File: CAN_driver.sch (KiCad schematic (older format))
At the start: 28 parts, among them J3 DB9_Male, J4 DB9_Male, J5 DB9_Male, J6 DB9_Male, U3 TCAN1042HVD, U5 TCAN1042HVD

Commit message: forgot to save schematic
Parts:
- J3, J4, J5, J6: footprint Connector_Dsub:DSUB-9_Male_Horizontal_P2.77x2.84mm_EdgePinOffset7.70mm_Housed_MountingHolesOffset9.12mm -> Connector_Dsub:DSUB-9_Male_Vertical_P2.77x2.84mm_MountingHoles
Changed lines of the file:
@@
 F 0 "J5" H 8130 4346 50  0000 L CNN
 F 1 "DB9_Male" H 8130 4255 50  0000 L CNN
-F 2 "Connector_Dsub:DSUB-9_Male_Horizontal_P2.77x2.84mm_EdgePinOffset7.70mm_Housed_MountingHolesOffset9.12mm" H 7950 4300 50  0001 C CNN
+F 2 "Connector_Dsub:DSUB-9_Male_Vertical_P2.77x2.84mm_MountingHoles" H 7950 4300 50  0001 C CNN
 F 3 " ~" H 7950 4300 50  0001 C CNN
 F 4 "5747840-3" H 7950 4300 50  0001 C CNN "Part"
@@
 F 0 "J6" H 8130 5496 50  0000 L CNN
 F 1 "DB9_Male" H 8130 5405 50  0000 L CNN
-F 2 "Connector_Dsub:DSUB-9_Male_Horizontal_P2.77x2.84mm_EdgePinOffset7.70mm_Housed_MountingHolesOffset9.12mm" H 7950 5450 50  0001 C CNN
+F 2 "Connector_Dsub:DSUB-9_Male_Vertical_P2.77x2.84mm_MountingHoles" H 7950 5450 50  0001 C CNN
 F 3 " ~" H 7950 5450 50  0001 C CNN
 F 4 "5747840-3" H 7950 5450 50  0001 C CNN "Part"
@@
 F 0 "J4" H 8130 2496 50  0000 L CNN
 F 1 "DB9_Male" H 8130 2405 50  0000 L CNN
-F 2 "Connector_Dsub:DSUB-9_Male_Horizontal_P2.77x2.84mm_EdgePinOffset7.70mm_Housed_MountingHolesOffset9.12mm" H 7950 2450 50  0001 C CNN
+F 2 "Connector_Dsub:DSUB-9_Male_Vertical_P2.77x2.84mm_MountingHoles" H 7950 2450 50  0001 C CNN
 F 3 " ~" H 7950 2450 50  0001 C CNN
 F 4 "5747840-3" H 7950 2450 50  0001 C CNN "Part"
@@
 F 0 "J3" H 8130 1346 50  0000 L CNN
 F 1 "DB9_Male" H 8130 1255 50  0000 L CNN
-F 2 "Connector_Dsub:DSUB-9_Male_Horizontal_P2.77x2.84mm_EdgePinOffset7.70mm_Housed_MountingHolesOffset9.12mm" H 7950 1300 50  0001 C CNN
+F 2 "Connector_Dsub:DSUB-9_Male_Vertical_P2.77x2.84mm_MountingHoles" H 7950 1300 50  0001 C CNN
 F 3 " ~" H 7950 1300 50  0001 C CNN
 F 4 "5747840-3" H 7950 1300 50  0001 C CNN "Part"

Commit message: decouple caps, moved testpoint for usb access, tcan footprints
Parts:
- U3, U5: footprint Package_SO:SOIC-8-1EP_3.9x4.9mm_P1.27mm_EP2.41x3.81mm -> Package_SO:SO-8_3.9x4.9mm_P1.27mm
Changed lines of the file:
@@
 BBCAN+
-$Comp
-L TCAN:TCAN1042HVD U3
-U 1 1 5E4AADCC
-P 3650 1300
-F 0 "U3" H 4450 1687 60  0000 C CNN
-F 1 "TCAN1042HVD" H 4450 1581 60  0000 C CNN
-F 2 "Package_SO:SOIC-8-1EP_3.9x4.9mm_P1.27mm_EP2.41x3.81mm" H 4450 1540 60  0001 C CNN
-F 3 "" H 3650 1300 60  0000 C CNN
-F 4 "296-48672-1-ND" H 3650 1300 50  0001 C CNN "Part"
-	1    3650 1300
-	1    0    0    -1
-$EndComp
 $Comp
 L power:GNDD #PWR?
@@
 F 0 "U5" H 4450 4587 60  0000 C CNN
 F 1 "TCAN1042HVD" H 4450 4481 60  0000 C CNN
-F 2 "Package_SO:SOIC-8-1EP_3.9x4.9mm_P1.27mm_EP2.41x3.81mm" H 4450 4440 60  0001 C CNN
+F 2 "Package_SO:SO-8_3.9x4.9mm_P1.27mm" H 4450 4440 60  0001 C CNN
 F 3 "" H 3650 4200 60  0000 C CNN
 F 4 "296-48672-1-ND" H 3650 4200 50  0001 C CNN "Part"
@@
 	1    0    0    -1
 $EndComp
+$Comp
+L TCAN:TCAN1042HVD U3
+U 1 1 5E4AADCC
+P 3650 1300
+F 0 "U3" H 4450 1687 60  0000 C CNN
+F 1 "TCAN1042HVD" H 4450 1581 60  0000 C CNN
+F 2 "Package_SO:SO-8_3.9x4.9mm_P1.27mm" H 4450 1540 60  0001 C CNN
+F 3 "" H 3650 1300 60  0000 C CNN
+F 4 "296-48672-1-ND" H 3650 1300 50  0001 C CNN "Part"
+	1    3650 1300
+	1    0    0    -1
+$EndComp

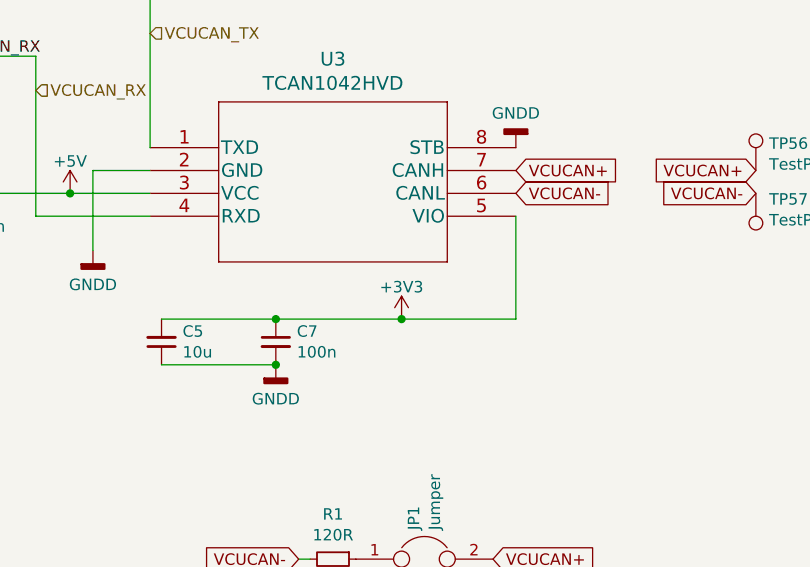
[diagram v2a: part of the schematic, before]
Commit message: better routing, tcan footprint, mount holes + silkscreen
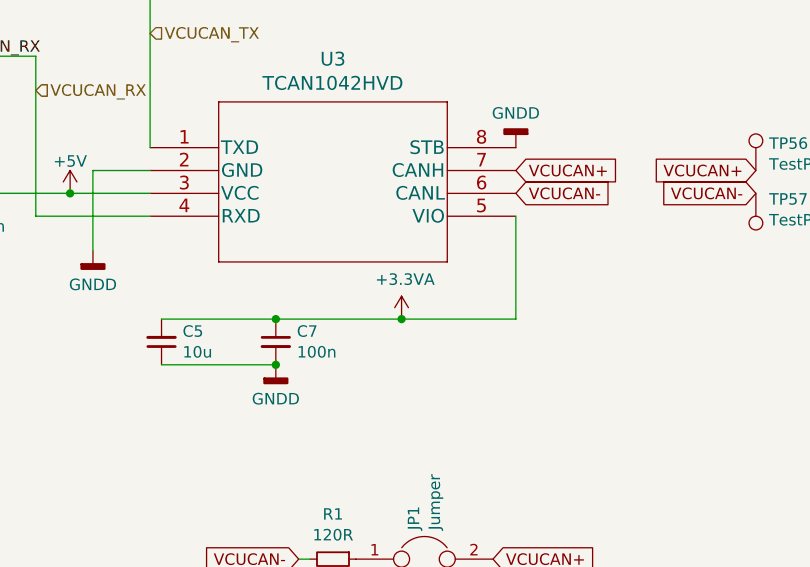
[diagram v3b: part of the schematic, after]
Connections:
- net +3V3: no longer C5.2, C7.1, U3.5 (VIO)
- new net +3.3VA: C5.2, C7.1, U3.5 (VIO)
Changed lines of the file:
@@
 $EndComp
 Connection ~ 4200 2050
-Connection ~ 4750 2050
 Wire Wire Line
 	2750 1500 3300 1500
@@
 Wire Wire Line
 	3650 1500 3300 1500
-$Comp
-L power:+3.3V #PWR?
-U 1 1 5E53D641
-P 4750 2050
-AR Path="/5E53D641" Ref="#PWR?"  Part="1"
-AR Path="/5ED986AC/5E53D641" Ref="#PWR0119"  Part="1"
-F 0 "#PWR0119" H 4750 1900 50  0001 C CNN
-F 1 "+3V3" H 4750 2190 50  0000 C CNN
-F 2 "" H 4750 2050 60  0000 C CNN
-F 3 "" H 4750 2050 60  0000 C CNN
-	1    4750 2050
-	1    0    0    -1
-$EndComp
 Text Label 2750 650  0    50   ~ 0
 VCUCAN_TX
@@
 VCUCAN_RX
 Wire Wire Line
-	4200 2050 4750 2050
-Wire Wire Line
 	5250 1600 5250 2050
-Wire Wire Line
-	4750 2050 5250 2050
 $Comp
 L power:GNDD #PWR?
@@
 $EndComp
 Connection ~ 4200 4950
-Connection ~ 4750 4950
 Wire Wire Line
 	2750 4400 3300 4400
@@
 Wire Wire Line
 	3650 4400 3300 4400
-$Comp
-L power:+3.3V #PWR?
-U 1 1 5E766408
-P 4750 4950
-AR Path="/5E766408" Ref="#PWR?"  Part="1"
-AR Path="/5ED986AC/5E766408" Ref="#PWR0131"  Part="1"
-F 0 "#PWR0131" H 4750 4800 50  0001 C CNN
-F 1 "+3V3" H 4750 5090 50  0000 C CNN
-F 2 "" H 4750 4950 60  0000 C CNN
-F 3 "" H 4750 4950 60  0000 C CNN
-	1    4750 4950
-	1    0    0    -1
-$EndComp
 Text Label 2750 3550 0    50   ~ 0
 BBCAN_TX
@@
 BBCAN_RX
 Wire Wire Line
-	4200 4950 4750 4950
-Wire Wire Line
 	5250 4500 5250 4950
-Wire Wire Line
-	4750 4950 5250 4950
 $Comp
 L power:GNDD #PWR?
@@
 	1    0    0    -1
 $EndComp
+Wire Wire Line
+	4750 4950 5250 4950
+Wire Wire Line
+	4200 4950 4750 4950
+Connection ~ 4750 4950
+$Comp
+L power:+3.3V #PWR?
+U 1 1 5E766408
+P 4750 4950
+AR Path="/5E766408" Ref="#PWR?"  Part="1"
+AR Path="/5ED986AC/5E766408" Ref="#PWR0131"  Part="1"
+F 0 "#PWR0131" H 4750 4800 50  0001 C CNN
+F 1 "+3V3" H 4750 5090 50  0000 C CNN
+F 2 "" H 4750 4950 60  0000 C CNN
+F 3 "" H 4750 4950 60  0000 C CNN
+	1    4750 4950
+	1    0    0    -1
+$EndComp
+Wire Wire Line
+	4200 2050 4750 2050
+$Comp
+L power:+3.3VA #PWR?
+U 1 1 5F34AABC
+P 4750 2050
+AR Path="/5F34AABC" Ref="#PWR?"  Part="1"
+AR Path="/5ED986AC/5F34AABC" Ref="#PWR0115"  Part="1"
+F 0 "#PWR0115" H 4750 1900 50  0001 C CNN
+F 1 "+3.3VA" H 4765 2223 50  0000 C CNN
+F 2 "" H 4750 2050 50  0001 C CNN
+F 3 "" H 4750 2050 50  0001 C CNN
+	1    4750 2050
+	1    0    0    -1
+$EndComp
+Connection ~ 4750 2050
+Wire Wire Line
+	4750 2050 5250 2050
 $EndSCHEMATC

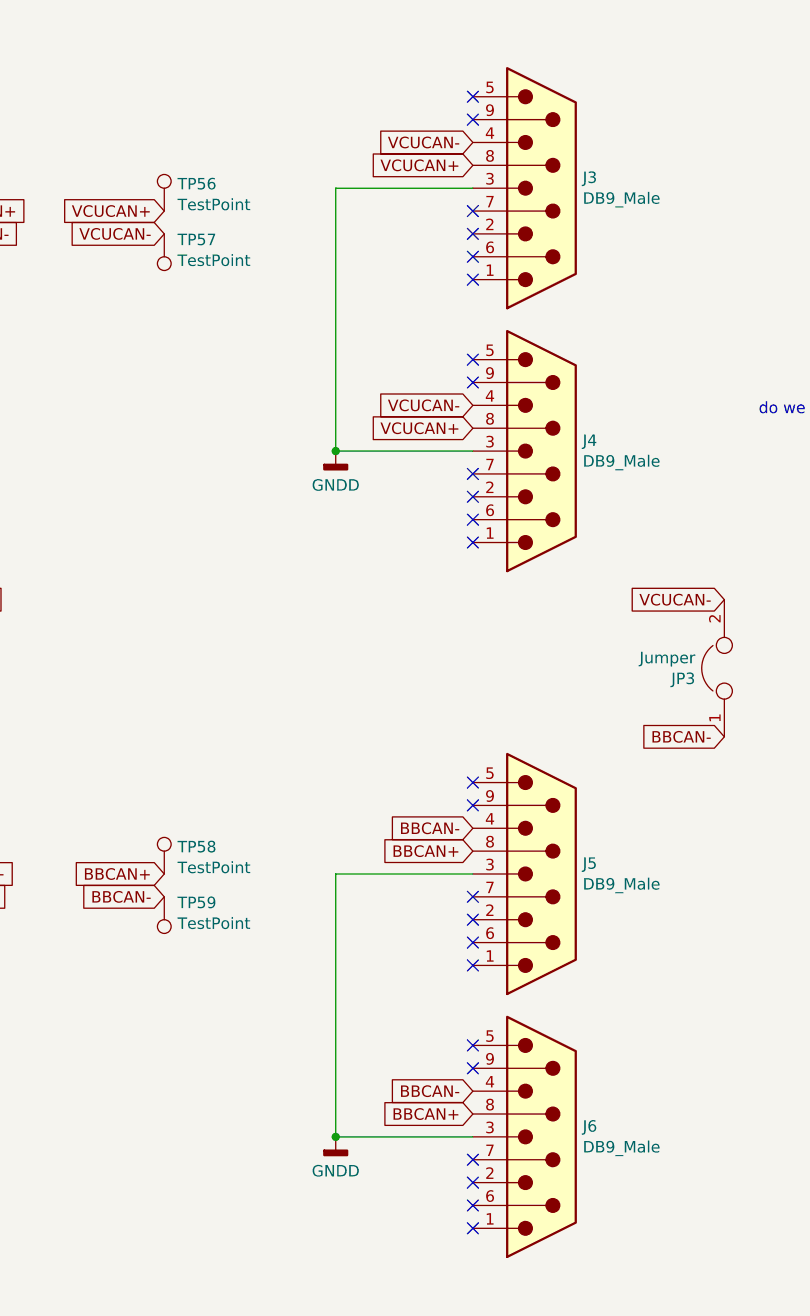
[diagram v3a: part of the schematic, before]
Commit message: rs232/can fix
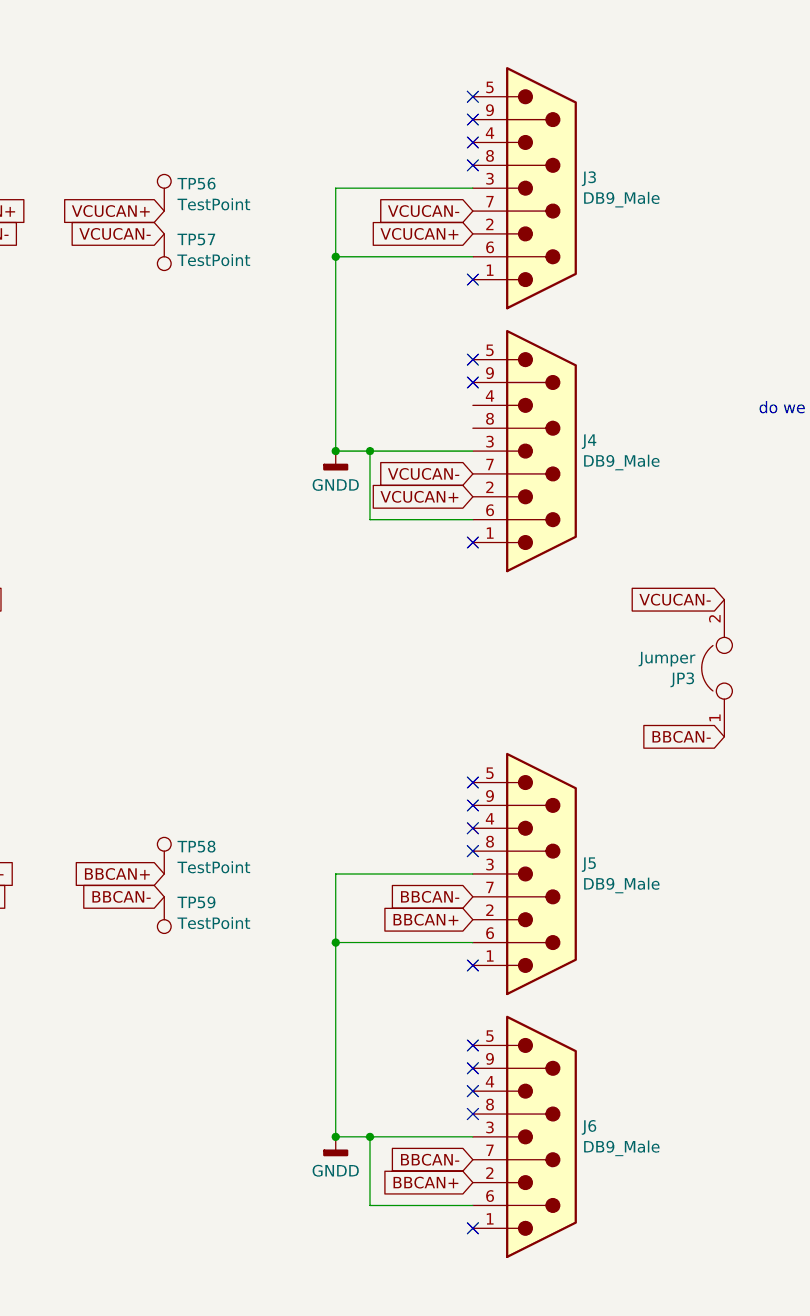
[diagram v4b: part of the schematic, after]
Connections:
- net BBCAN+: now also J5.2, J6.2; no longer J5.8, J6.8
- net BBCAN-: now also J5.7, J6.7; no longer J5.4, J6.4
- net GNDD: now also J3.6, J4.6, J5.6, J6.6
- net VCUCAN+: now also J3.2, J4.2; no longer J3.8, J4.8
- net VCUCAN-: now also J3.7, J4.7; no longer J3.4, J4.4
- no-connect marks 24 -> 18
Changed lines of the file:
@@
 VCUCAN+
 Wire Wire Line
-	7050 5450 7650 5450
+	7050 5450 7200 5450
 Wire Wire Line
 	7650 4300 7050 4300
-Text GLabel 7650 5350 0    50   Input ~ 0
+Text GLabel 7650 5650 0    50   Input ~ 0
 BBCAN+
-Text GLabel 7650 4200 0    50   Input ~ 0
+Text GLabel 7650 4500 0    50   Input ~ 0
 BBCAN+
-Text GLabel 7650 5250 0    50   Input ~ 0
+Text GLabel 7650 5550 0    50   Input ~ 0
 BBCAN-
-Text GLabel 7650 4100 0    50   Input ~ 0
+Text GLabel 7650 4400 0    50   Input ~ 0
 BBCAN-
 $Comp
@@
 	1    0    0    -1
 $EndComp
-Text GLabel 7650 1100 0    50   Input ~ 0
+Text GLabel 7650 1400 0    50   Input ~ 0
 VCUCAN-
-Text GLabel 7650 2250 0    50   Input ~ 0
+Text GLabel 7650 2550 0    50   Input ~ 0
 VCUCAN-
-Text GLabel 7650 1200 0    50   Input ~ 0
+Text GLabel 7650 1500 0    50   Input ~ 0
 VCUCAN+
-Text GLabel 7650 2350 0    50   Input ~ 0
+Text GLabel 7650 2650 0    50   Input ~ 0
 VCUCAN+
 Wire Wire Line
 	7650 1300 7050 1300
 Wire Wire Line
-	7050 2450 7650 2450
+	7050 2450 7200 2450
 $Comp
 L Connector:TestPoint TP56
@@
 $EndComp
 Wire Wire Line
-	7050 1300 7050 2450
-Wire Wire Line
-	7050 4300 7050 5450
+	7050 1300 7050 1600
+Wire Wire Line
+	7050 4300 7050 4600
 $Comp
 L TCAN:TCAN1042HVD U5
@@
 NoConn ~ 7650 1000
 NoConn ~ 7650 900
-NoConn ~ 7650 1400
-NoConn ~ 7650 1500
-NoConn ~ 7650 1600
 NoConn ~ 7650 1700
 NoConn ~ 7650 2850
-NoConn ~ 7650 2750
-NoConn ~ 7650 2650
-NoConn ~ 7650 2550
 NoConn ~ 7650 2150
 NoConn ~ 7650 2050
 NoConn ~ 7650 4700
-NoConn ~ 7650 4600
-NoConn ~ 7650 4500
-NoConn ~ 7650 4400
 NoConn ~ 7650 4000
 NoConn ~ 7650 3900
@@
 NoConn ~ 7650 5050
 NoConn ~ 7650 5850
-NoConn ~ 7650 5750
-NoConn ~ 7650 5650
-NoConn ~ 7650 5550
 $Comp
 L Device:Jumper JP?
@@
 Wire Wire Line
 	4750 2050 5250 2050
+NoConn ~ 7650 5350
+NoConn ~ 7650 5250
+NoConn ~ 7650 4200
+NoConn ~ 7650 4100
+Wire Wire Line
+	7650 4600 7050 4600
+Connection ~ 7050 4600
+Wire Wire Line
+	7050 4600 7050 5450
+Wire Wire Line
+	7650 5750 7200 5750
+Wire Wire Line
+	7200 5750 7200 5450
+Connection ~ 7200 5450
+Wire Wire Line
+	7200 5450 7650 5450
+Wire Wire Line
+	7650 2750 7200 2750
+Wire Wire Line
+	7200 2750 7200 2450
+Connection ~ 7200 2450
+Wire Wire Line
+	7200 2450 7650 2450
+NoConn ~ 7650 1200
+NoConn ~ 7650 1100
+Wire Wire Line
+	7650 1600 7050 1600
+Connection ~ 7050 1600
+Wire Wire Line
+	7050 1600 7050 2450
 $EndSCHEMATC

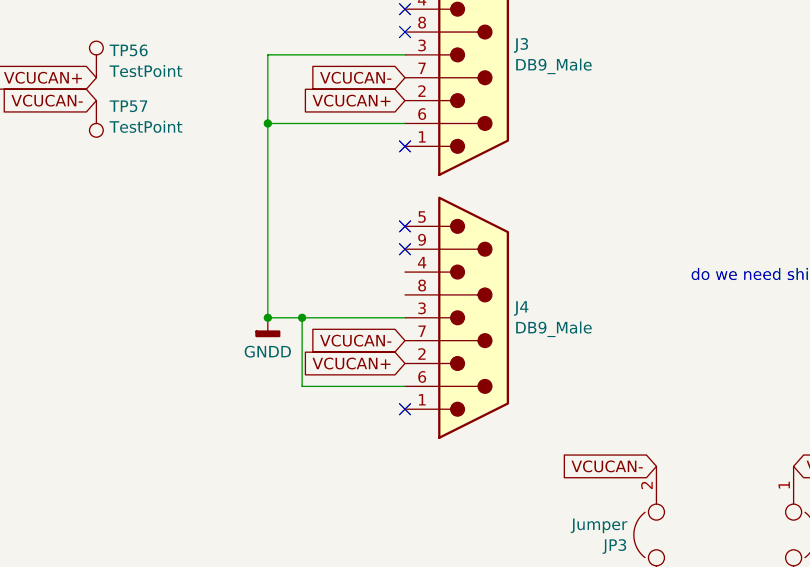
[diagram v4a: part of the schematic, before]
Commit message: gerbers and pdfs
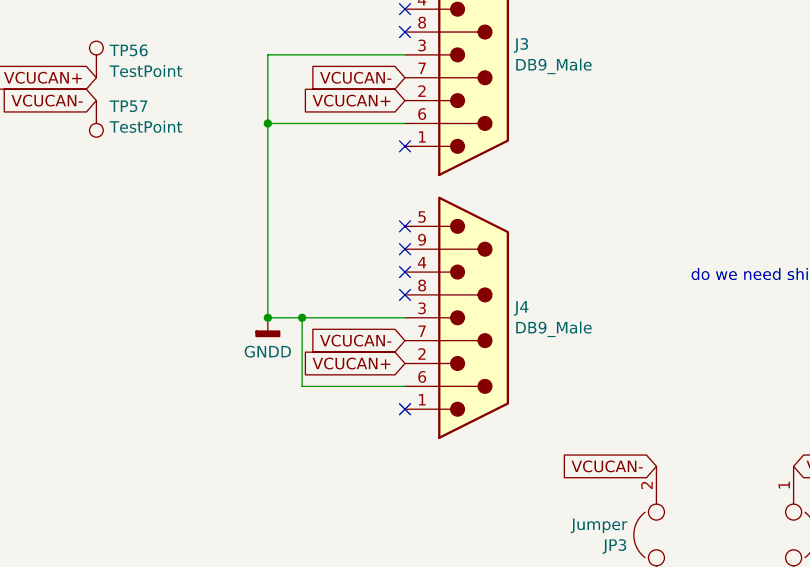
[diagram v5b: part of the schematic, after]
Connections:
- no-connect marks 18 -> 20
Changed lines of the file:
@@
 Wire Wire Line
 	7050 1600 7050 2450
+NoConn ~ 7650 2250
+NoConn ~ 7650 2350
 $EndSCHEMATC

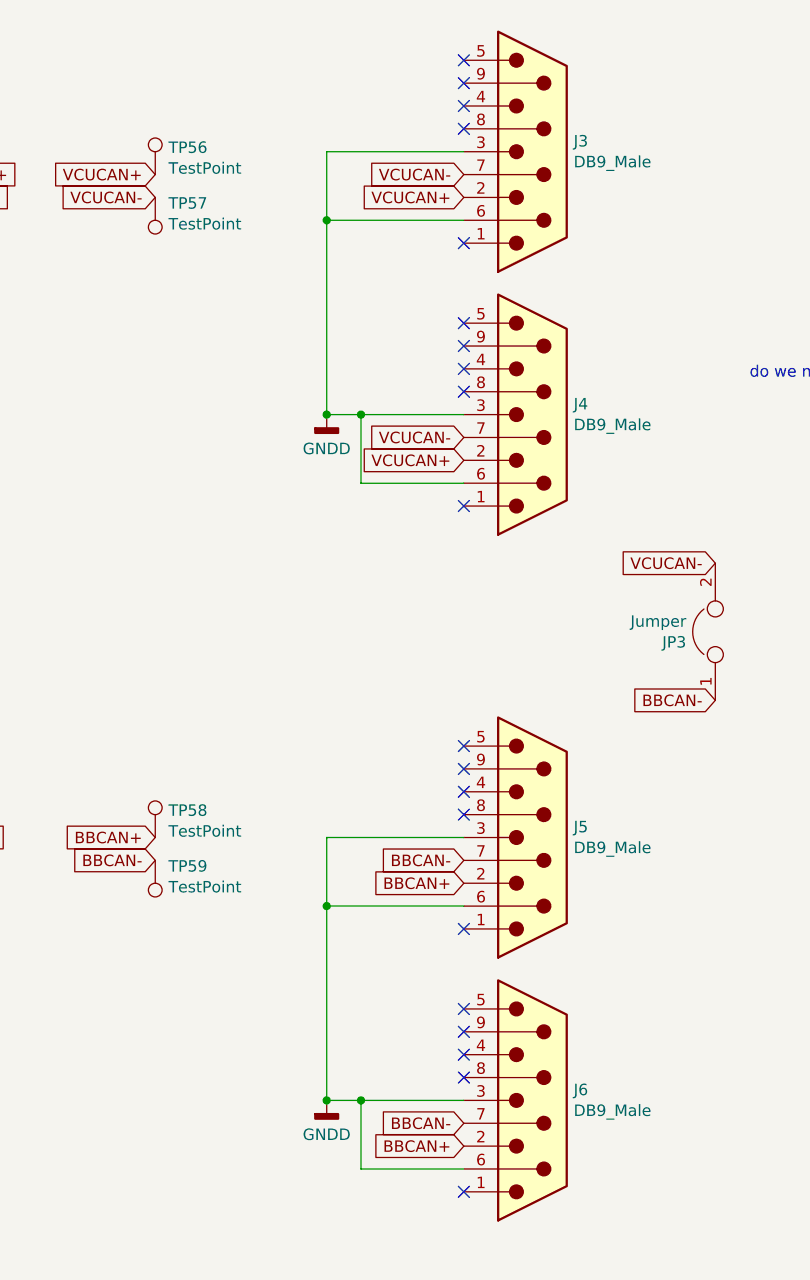
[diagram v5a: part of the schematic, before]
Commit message: CAN pin fix, need to ground pour and done
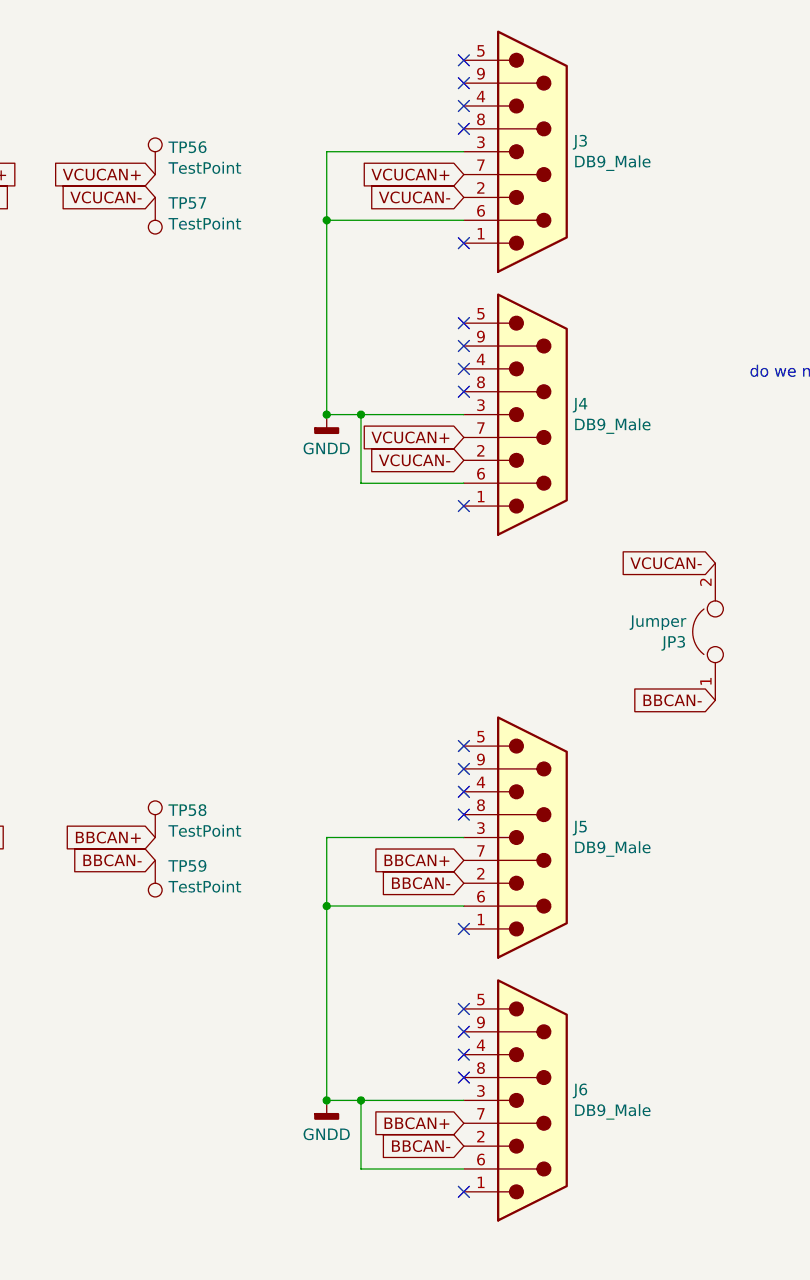
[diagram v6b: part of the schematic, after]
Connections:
- net BBCAN+: now also J5.7, J6.7; no longer J5.2, J6.2
- net BBCAN-: now also J5.2, J6.2; no longer J5.7, J6.7
- net VCUCAN+: now also J3.7, J4.7; no longer J3.2, J4.2
- net VCUCAN-: now also J3.2, J4.2; no longer J3.7, J4.7
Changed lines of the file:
@@
 Wire Wire Line
 	7650 4300 7050 4300
+Text GLabel 7650 5550 0    50   Input ~ 0
+BBCAN+
+Text GLabel 7650 4400 0    50   Input ~ 0
+BBCAN+
 Text GLabel 7650 5650 0    50   Input ~ 0
-BBCAN+
+BBCAN-
 Text GLabel 7650 4500 0    50   Input ~ 0
-BBCAN+
-Text GLabel 7650 5550 0    50   Input ~ 0
-BBCAN-
-Text GLabel 7650 4400 0    50   Input ~ 0
 BBCAN-
 $Comp
@@
 	1    0    0    -1
 $EndComp
+Text GLabel 7650 1500 0    50   Input ~ 0
+VCUCAN-
+Text GLabel 7650 2650 0    50   Input ~ 0
+VCUCAN-
 Text GLabel 7650 1400 0    50   Input ~ 0
-VCUCAN-
+VCUCAN+
 Text GLabel 7650 2550 0    50   Input ~ 0
-VCUCAN-
-Text GLabel 7650 1500 0    50   Input ~ 0
-VCUCAN+
-Text GLabel 7650 2650 0    50   Input ~ 0
 VCUCAN+
 Wire Wire Line
